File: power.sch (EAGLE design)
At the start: 37 parts, among them IC1 74HC125D, IC2 7805TV, IC3 7815TV

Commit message: wait for the next one...
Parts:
- removed D5: AA215, diode:AA215
- added OK1: 4N35M, optocoupler:4N35M
- D4: value AA215 -> 1N4446; device diode:AA215 -> diode:1N4446
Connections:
- removed net N$14: D4.C, D5.A, U$6.GNDA_ADC
- new net N$31: OK1.A, R12.2
- net GND: now also OK1.BAS, OK1.C, U$6.AIN1
- net N$26: now also D4.C, OK1.COL, U$6.GNDA_ADC; no longer D5.C, R12.1
- net N$8: no longer R12.2
- net VCC: now also R12.1
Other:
- note added: "vref diode (trust me, this works)"
- note removed: "vref diode"
- moved on the sheet: D4, R12
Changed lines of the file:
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@@
 <part name="H3" library="holes" deviceset="MOUNT-PAD-ROUND" device="2.8"/>
 <part name="R7" library="rcl" deviceset="R-US_" device="R0603" value="15k"/>
-<part name="D4" library="diode" deviceset="AA215" device=""/>
 <part name="R12" library="rcl" deviceset="R-US_" device="R0603" value="1k"/>
 <part name="GND7" library="supply1" deviceset="GND" device=""/>
@@
 <part name="P+1" library="supply1" deviceset="VCC" device=""/>
 <part name="P+2" library="supply1" deviceset="VCC" device=""/>
-<part name="D5" library="diode" deviceset="AA215" device=""/>
+<part name="P+3" library="supply1" deviceset="VCC" device=""/>
+<part name="OK1" library="optocoupler" deviceset="4N*?M" device="" technology="35"/>
+<part name="D4" library="diode" deviceset="1N4446" device=""/>
+<part name="GND11" library="supply1" deviceset="GND" device=""/>
+<part name="GND12" library="supply1" deviceset="GND" device=""/>
 </parts>
 <sheets>
@@
 <plain>
 <text x="22.86" y="-2.54" size="1.778" layer="91">need gate drivers?</text>
-<text x="-40.64" y="27.94" size="1.778" layer="91" rot="R90">vref diode</text>
+<text x="-22.86" y="-53.34" size="1.778" layer="91" rot="R90">vref diode
+(trust me, this works)</text>
 <text x="86.36" y="-30.48" size="1.778" layer="91">Note: these pins are
 to be connected to
@@
 <instance part="H3" gate="G$1" x="142.24" y="73.66"/>
 <instance part="R7" gate="G$1" x="109.22" y="99.06" rot="R270"/>
-<instance part="D4" gate="1" x="-38.1" y="30.48" smashed="yes" rot="R90">
-<attribute name="NAME" x="-41.1226" y="27.94" size="1.778" layer="95" rot="R90"/>
-<attribute name="VALUE" x="-33.2486" y="25.4" size="1.778" layer="96" rot="R90"/>
-</instance>
-<instance part="R12" gate="G$1" x="-38.1" y="50.8" rot="R90"/>
-<instance part="GND7" gate="1" x="-38.1" y="22.86"/>
+<instance part="R12" gate="G$1" x="-63.5" y="-35.56" rot="R270"/>
+<instance part="GND7" gate="1" x="-63.5" y="-58.42"/>
 <instance part="IC1" gate="D" x="15.24" y="27.94" rot="MR180"/>
 <instance part="IC1" gate="A" x="15.24" y="63.5" rot="MR180"/>
@@
 <instance part="P+1" gate="VCC" x="-2.54" y="129.54" rot="R270"/>
 <instance part="P+2" gate="VCC" x="71.12" y="-20.32"/>
-<instance part="D5" gate="1" x="-38.1" y="40.64" smashed="yes" rot="R90">
-<attribute name="NAME" x="-41.1226" y="38.1" size="1.778" layer="95" rot="R90"/>
-<attribute name="VALUE" x="-33.2486" y="35.56" size="1.778" layer="96" rot="R90"/>
-</instance>
+<instance part="P+3" gate="VCC" x="-63.5" y="-25.4"/>
+<instance part="OK1" gate="G$1" x="-48.26" y="-45.72"/>
+<instance part="D4" gate="1" x="-33.02" y="-48.26" rot="R270"/>
+<instance part="GND11" gate="1" x="-33.02" y="-35.56" rot="R180"/>
+<instance part="GND12" gate="1" x="17.78" y="-111.76"/>
 </instances>
 <busses>
@@
 <segment>
 <pinref part="GND7" gate="1" pin="GND"/>
-<pinref part="D4" gate="1" pin="A"/>
-<wire x1="-38.1" y1="25.4" x2="-38.1" y2="27.94" width="0.1524" layer="91"/>
+<wire x1="-63.5" y1="-55.88" x2="-63.5" y2="-50.8" width="0.1524" layer="91"/>
+<pinref part="OK1" gate="G$1" pin="C"/>
+<wire x1="-63.5" y1="-50.8" x2="-58.42" y2="-50.8" width="0.1524" layer="91"/>
 </segment>
 <segment>
@@
 <junction x="-43.18" y="109.22"/>
 <junction x="-20.32" y="109.22"/>
+</segment>
+<segment>
+<pinref part="D4" gate="1" pin="A"/>
+<wire x1="-33.02" y1="-45.72" x2="-33.02" y2="-43.18" width="0.1524" layer="91"/>
+<wire x1="-33.02" y1="-43.18" x2="-40.64" y2="-43.18" width="0.1524" layer="91"/>
+<pinref part="OK1" gate="G$1" pin="BAS"/>
+<pinref part="GND11" gate="1" pin="GND"/>
+<wire x1="-33.02" y1="-38.1" x2="-33.02" y2="-43.18" width="0.1524" layer="91"/>
+<junction x="-33.02" y="-43.18"/>
+</segment>
+<segment>
+<pinref part="U$6" gate="G$1" pin="AIN1"/>
+<pinref part="GND12" gate="1" pin="GND"/>
+<wire x1="17.78" y1="-91.44" x2="17.78" y2="-109.22" width="0.1524" layer="91"/>
 </segment>
 </net>
@@
 <wire x1="-50.8" y1="55.88" x2="-50.8" y2="58.42" width="0.1524" layer="91"/>
 <pinref part="U$8" gate="G$1" pin="S"/>
-<wire x1="-38.1" y1="58.42" x2="-17.78" y2="58.42" width="0.1524" layer="91"/>
-<wire x1="-17.78" y1="58.42" x2="-17.78" y2="76.2" width="0.1524" layer="91"/>
-<wire x1="40.64" y1="76.2" x2="-17.78" y2="76.2" width="0.1524" layer="91"/>
-<wire x1="-38.1" y1="58.42" x2="-38.1" y2="55.88" width="0.1524" layer="91"/>
-<pinref part="R12" gate="G$1" pin="2"/>
+<wire x1="-38.1" y1="58.42" x2="-15.24" y2="58.42" width="0.1524" layer="91"/>
+<wire x1="-15.24" y1="58.42" x2="-15.24" y2="76.2" width="0.1524" layer="91"/>
+<wire x1="40.64" y1="76.2" x2="-15.24" y2="76.2" width="0.1524" layer="91"/>
 <pinref part="U$7" gate="G$1" pin="S"/>
-<wire x1="35.56" y1="91.44" x2="-17.78" y2="91.44" width="0.1524" layer="91"/>
-<wire x1="-17.78" y1="91.44" x2="-17.78" y2="76.2" width="0.1524" layer="91"/>
-<junction x="-17.78" y="76.2"/>
+<wire x1="35.56" y1="91.44" x2="-15.24" y2="91.44" width="0.1524" layer="91"/>
+<wire x1="-15.24" y1="91.44" x2="-15.24" y2="76.2" width="0.1524" layer="91"/>
+<junction x="-15.24" y="76.2"/>
 <wire x1="-53.34" y1="58.42" x2="-38.1" y2="58.42" width="0.1524" layer="91"/>
 <junction x="-50.8" y="58.42"/>
@@
 <net name="N$12" class="0">
 <segment>
-<wire x1="-27.94" y1="-7.62" x2="20.32" y2="-7.62" width="0.1524" layer="91"/>
+<wire x1="-17.78" y1="-7.62" x2="20.32" y2="-7.62" width="0.1524" layer="91"/>
 <wire x1="20.32" y1="-7.62" x2="20.32" y2="-35.56" width="0.1524" layer="91"/>
 <pinref part="R4" gate="G$1" pin="2"/>
@@
 <wire x1="-66.04" y1="81.28" x2="-66.04" y2="78.74" width="0.1524" layer="91"/>
 <junction x="-66.04" y="81.28"/>
-<wire x1="-66.04" y1="81.28" x2="-27.94" y2="81.28" width="0.1524" layer="91"/>
-<wire x1="-27.94" y1="81.28" x2="-27.94" y2="-7.62" width="0.1524" layer="91"/>
+<wire x1="-66.04" y1="81.28" x2="-17.78" y2="81.28" width="0.1524" layer="91"/>
+<wire x1="-17.78" y1="81.28" x2="-17.78" y2="-7.62" width="0.1524" layer="91"/>
 <pinref part="U$6" gate="G$1" pin="AIN2"/>
-</segment>
-</net>
-<net name="N$14" class="0">
-<segment>
-<pinref part="U$6" gate="G$1" pin="GNDA_ADC"/>
-<wire x1="25.4" y1="-91.44" x2="25.4" y2="-99.06" width="0.1524" layer="91"/>
-<wire x1="25.4" y1="-99.06" x2="-33.02" y2="-99.06" width="0.1524" layer="91"/>
-<wire x1="-33.02" y1="-99.06" x2="-33.02" y2="35.56" width="0.1524" layer="91"/>
-<wire x1="-33.02" y1="35.56" x2="-38.1" y2="35.56" width="0.1524" layer="91"/>
-<pinref part="D4" gate="1" pin="C"/>
-<wire x1="-38.1" y1="35.56" x2="-38.1" y2="33.02" width="0.1524" layer="91"/>
-<junction x="-38.1" y="35.56"/>
-<pinref part="D5" gate="1" pin="A"/>
-<wire x1="-38.1" y1="38.1" x2="-38.1" y2="35.56" width="0.1524" layer="91"/>
 </segment>
 </net>
@@
 <junction x="71.12" y="-27.94"/>
 </segment>
+<segment>
+<pinref part="R12" gate="G$1" pin="1"/>
+<pinref part="P+3" gate="VCC" pin="VCC"/>
+<wire x1="-63.5" y1="-30.48" x2="-63.5" y2="-27.94" width="0.1524" layer="91"/>
+</segment>
 </net>
 <net name="N$2" class="0">
@@
 <pinref part="D1" gate="1" pin="A"/>
 <wire x1="76.2" y1="106.68" x2="86.36" y2="106.68" width="0.1524" layer="91"/>
-</segment>
-</net>
-<net name="N$26" class="0">
-<segment>
-<pinref part="R12" gate="G$1" pin="1"/>
-<wire x1="-38.1" y1="45.72" x2="-38.1" y2="43.18" width="0.1524" layer="91"/>
-<pinref part="D5" gate="1" pin="C"/>
 </segment>
 </net>
@@
 </segment>
 </net>
+<net name="N$26" class="0">
+<segment>
+<pinref part="OK1" gate="G$1" pin="COL"/>
+<wire x1="-40.64" y1="-45.72" x2="-38.1" y2="-45.72" width="0.1524" layer="91"/>
+<wire x1="-38.1" y1="-45.72" x2="-38.1" y2="-53.34" width="0.1524" layer="91"/>
+<wire x1="-38.1" y1="-53.34" x2="-33.02" y2="-53.34" width="0.1524" layer="91"/>
+<pinref part="D4" gate="1" pin="C"/>
+<wire x1="-33.02" y1="-53.34" x2="-33.02" y2="-50.8" width="0.1524" layer="91"/>
+<pinref part="U$6" gate="G$1" pin="GNDA_ADC"/>
+<wire x1="25.4" y1="-91.44" x2="25.4" y2="-99.06" width="0.1524" layer="91"/>
+<wire x1="25.4" y1="-99.06" x2="-33.02" y2="-99.06" width="0.1524" layer="91"/>
+<wire x1="-33.02" y1="-99.06" x2="-33.02" y2="-53.34" width="0.1524" layer="91"/>
+<junction x="-33.02" y="-53.34"/>
+</segment>
+</net>
+<net name="N$31" class="0">
+<segment>
+<pinref part="R12" gate="G$1" pin="2"/>
+<wire x1="-63.5" y1="-40.64" x2="-63.5" y2="-43.18" width="0.1524" layer="91"/>
+<pinref part="OK1" gate="G$1" pin="A"/>
+<wire x1="-63.5" y1="-43.18" x2="-58.42" y2="-43.18" width="0.1524" layer="91"/>
+</segment>
+</net>

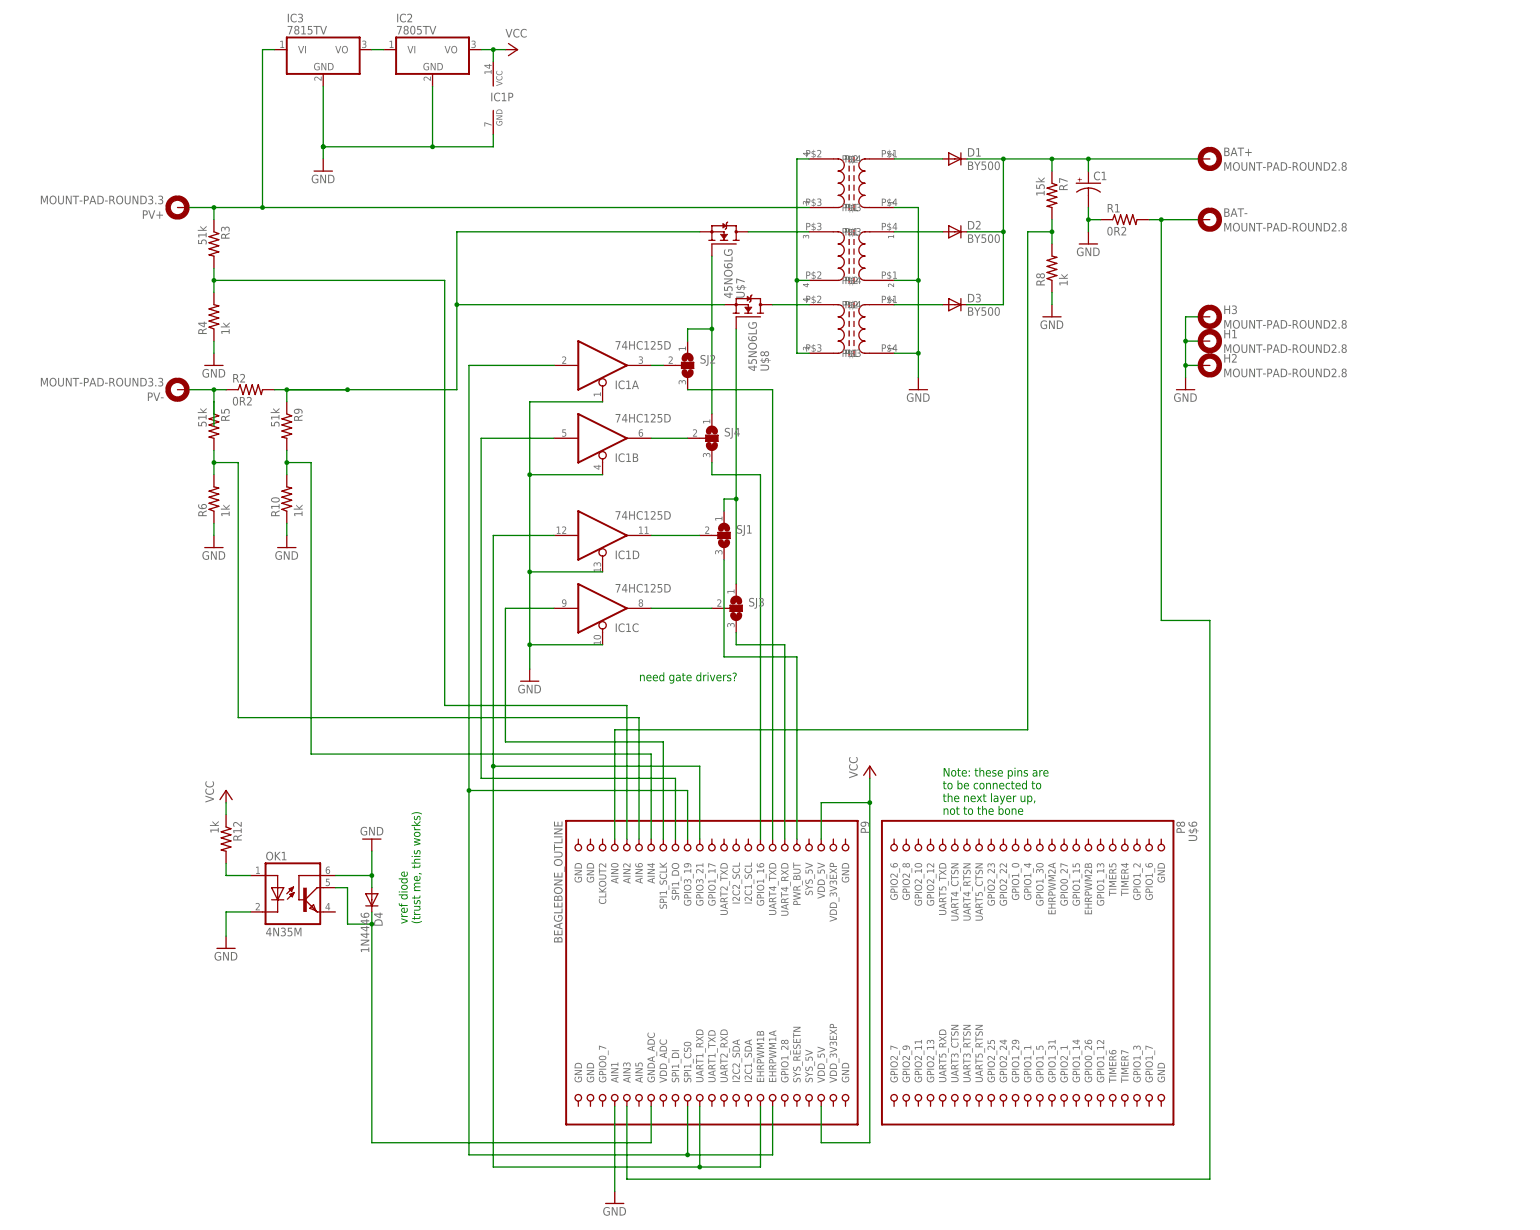
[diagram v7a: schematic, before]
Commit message: Removing all the failed ideas
Everything may be broken
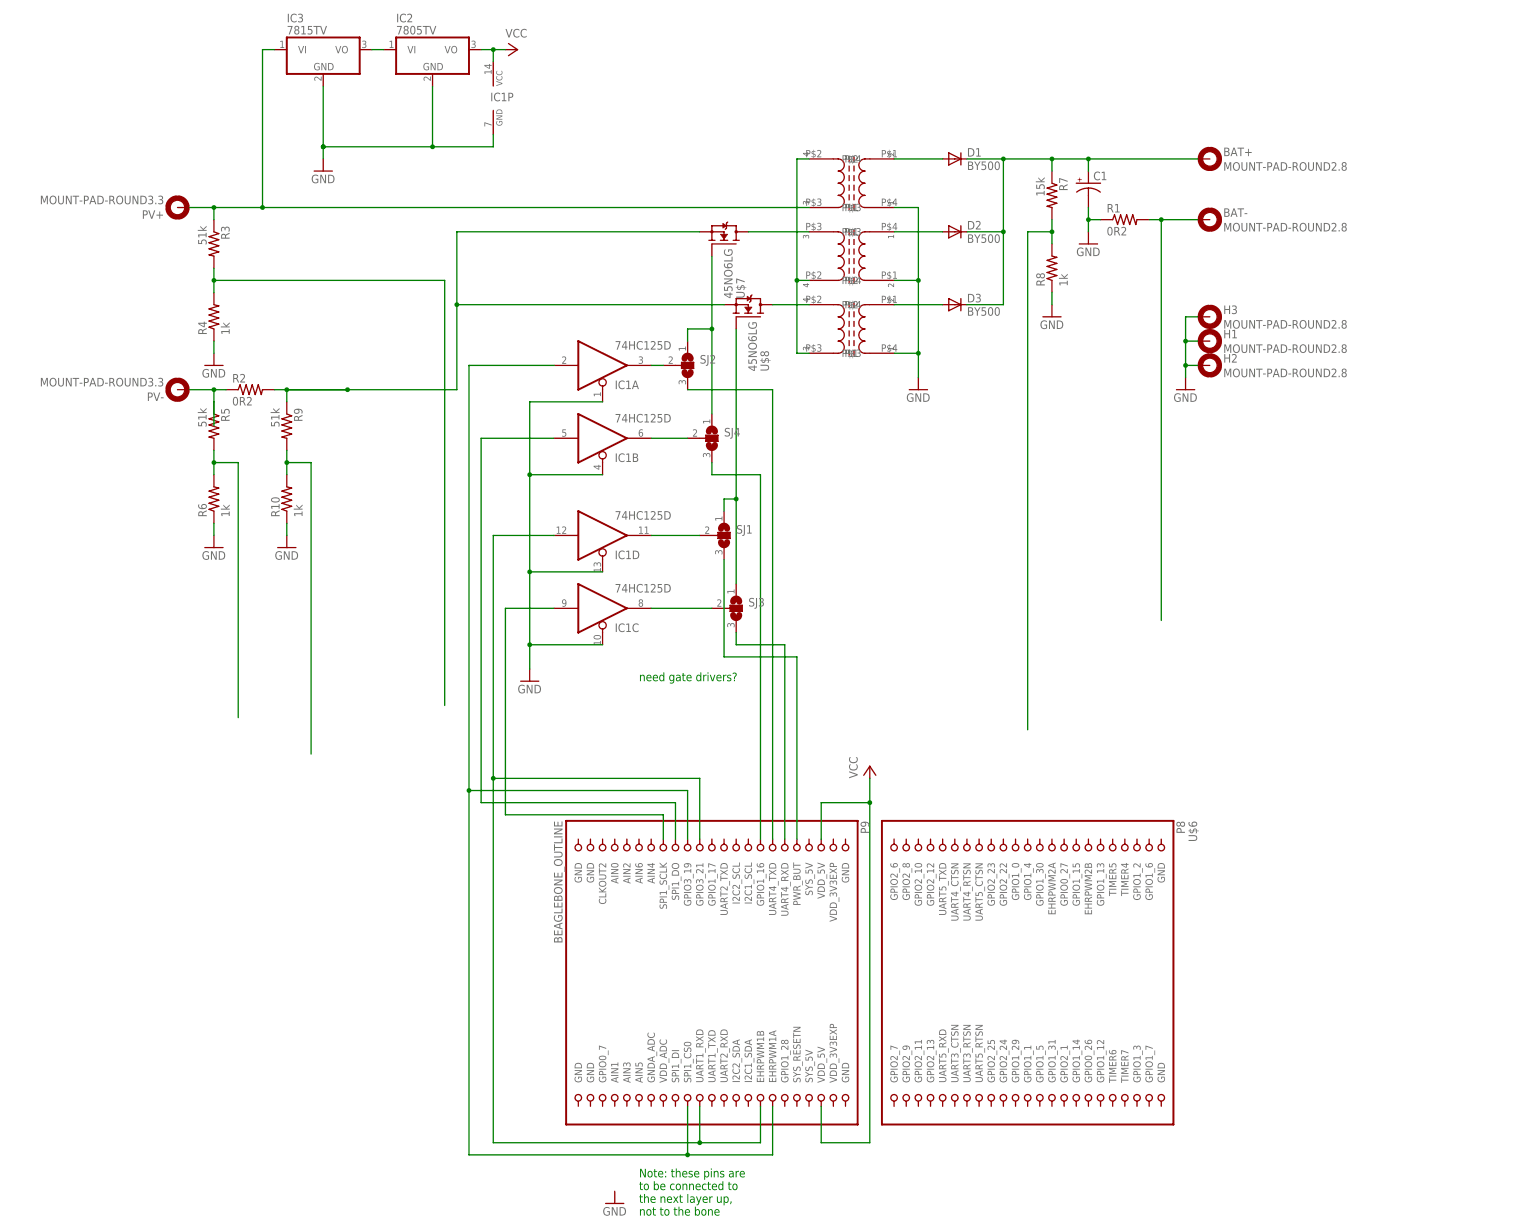
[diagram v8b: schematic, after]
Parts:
- removed D4: 1N4446, diode:1N4446
- removed OK1: 4N35M, optocoupler:4N35M
- removed R12: 1k, rcl:R-US_R0603
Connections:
- removed net N$26: D4.C, OK1.COL, U$6.GNDA_ADC
- removed net N$31: OK1.A, R12.2
- net GND: no longer D4.A, OK1.BAS, OK1.C, U$6.AIN1
- net N$10: no longer U$6.AIN0
- net N$12: no longer U$6.AIN2
- net N$17: no longer U$6.AIN6
- net N$18: no longer U$6.AIN4
- net N$4: no longer U$6.AIN3
- net VCC: no longer R12.1
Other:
- note removed: "vref diode (trust me, this works)"
